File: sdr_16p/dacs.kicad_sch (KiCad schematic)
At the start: 2 parts, among them U15 HMC7043LP7FE, U9 AD9508BCPZ

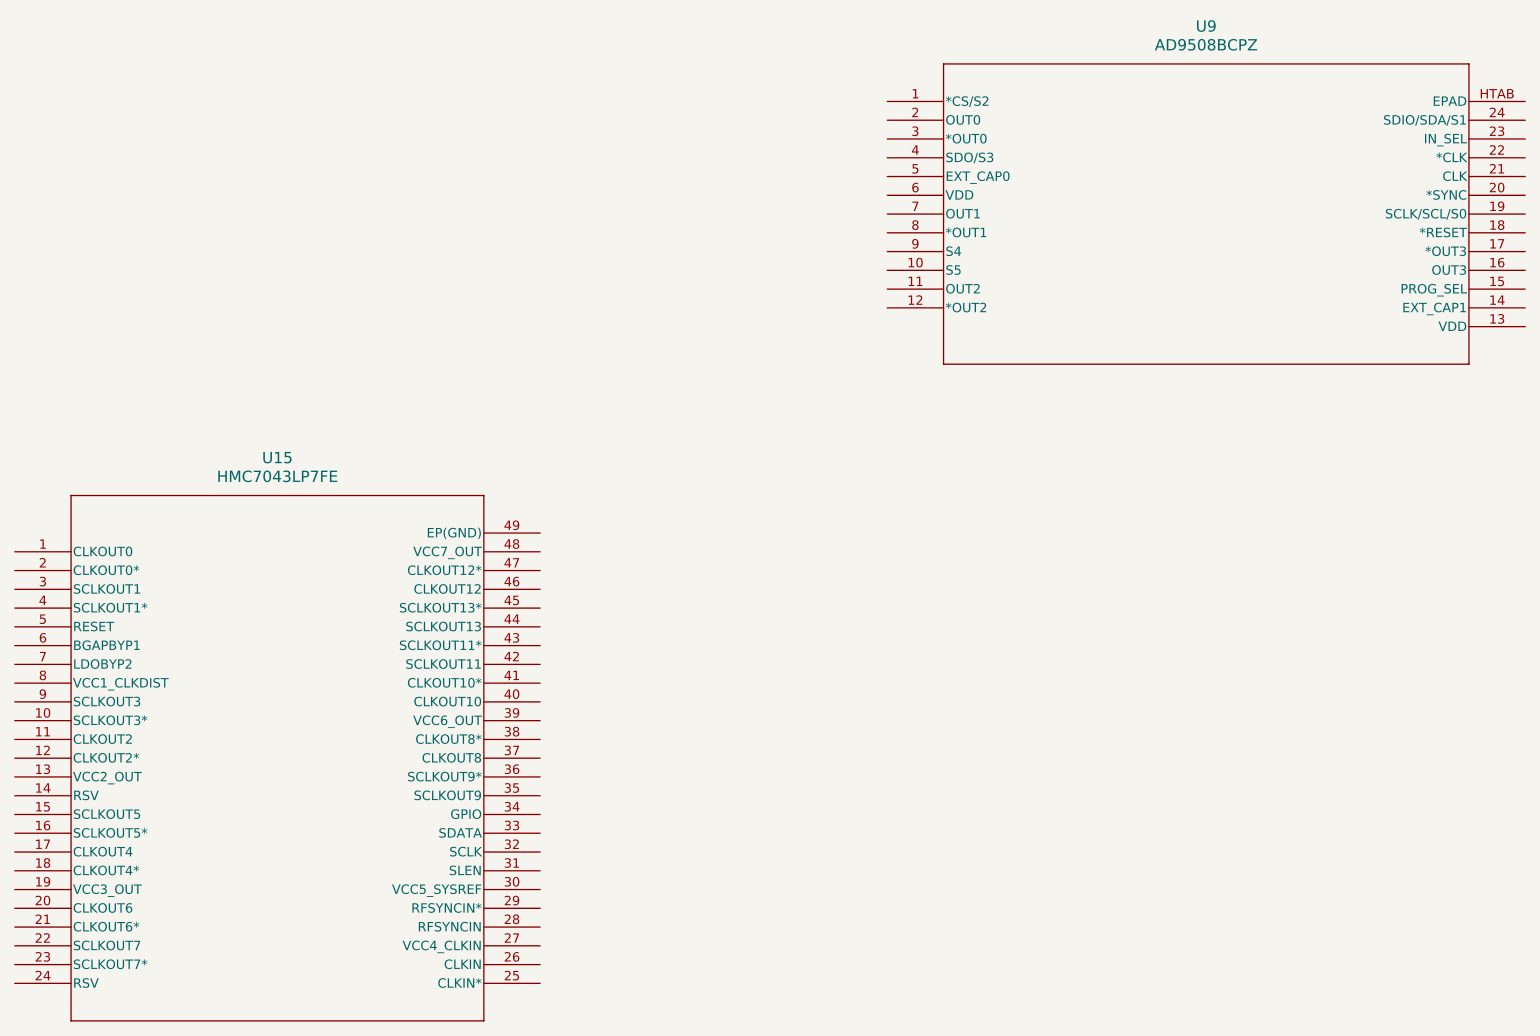
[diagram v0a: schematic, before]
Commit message: back to 16 phases
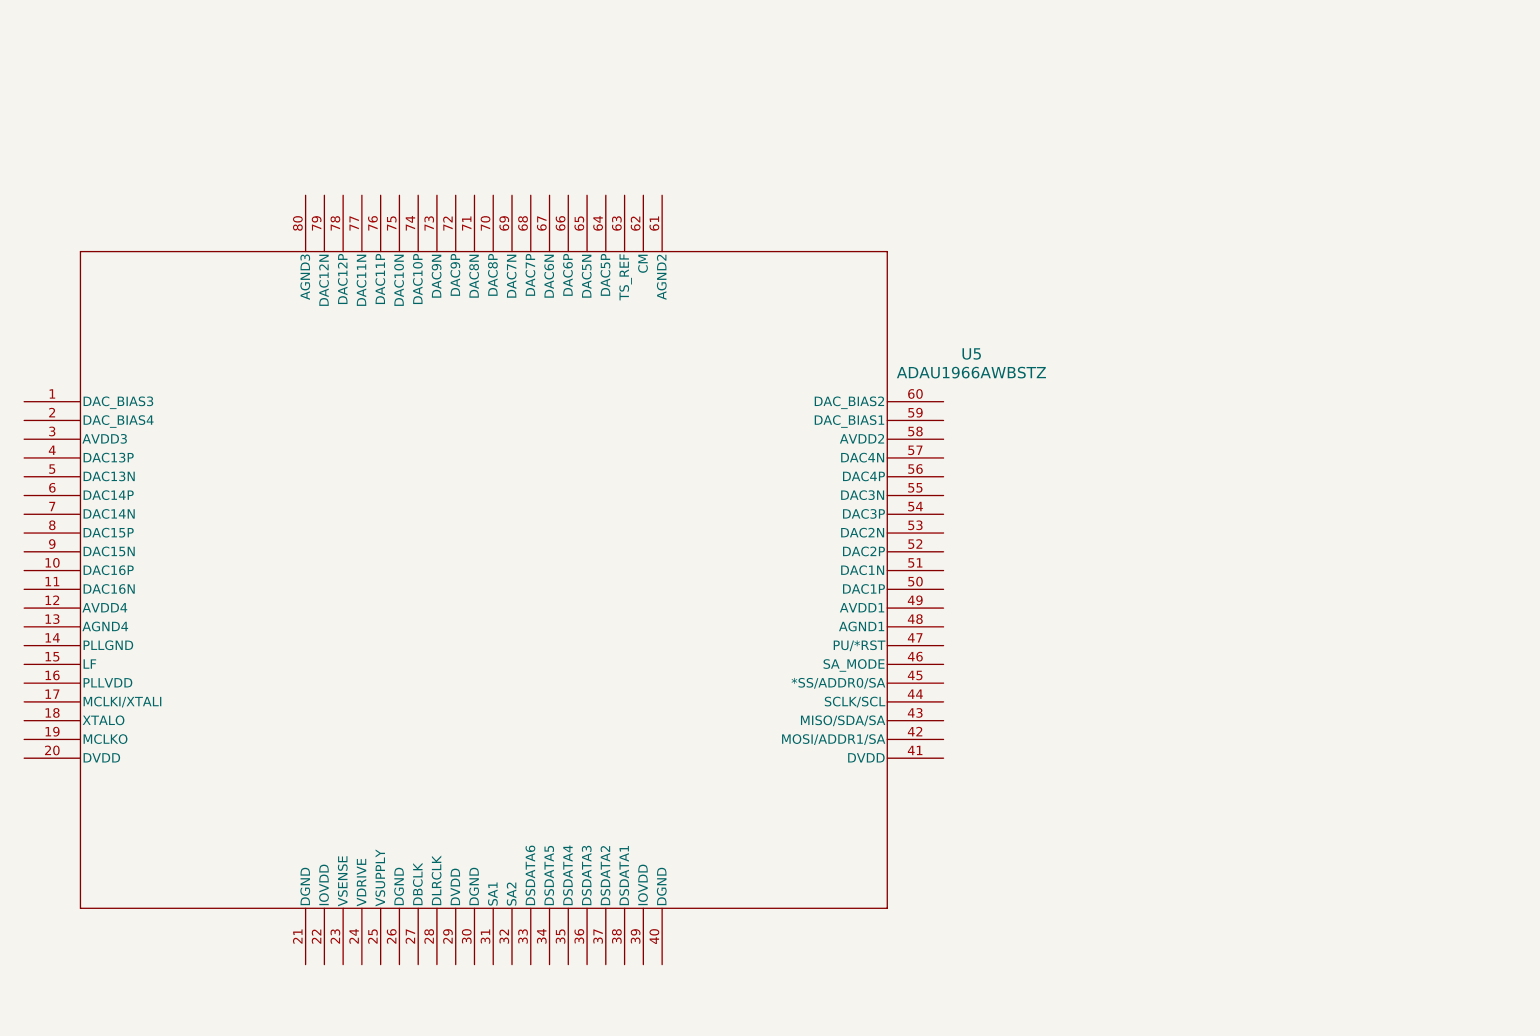
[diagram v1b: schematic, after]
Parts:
- removed U15: HMC7043LP7FE, HCP_48_1_ADI, symbol HMC7043:HMC7043LP7FE
- removed U9: AD9508BCPZ, CP_24_7_ADI, symbol AD9508:AD9508BCPZ
- added U5: ADAU1966AWBSTZ, ST_80_2_ADI, symbol ADAU1966:ADAU1966AWBSTZ
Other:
- title: Clock Tree -> Transmit DACs
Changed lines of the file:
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@@
 	(paper "B")
 	(title_block
-		(title "Clock Tree")
-		(date "2025-12-31")
+		(title "Transmit DACs")
+		(date "2026-01-02")
 		(rev "0.0")
 		(company "Andy McCann KA3KAF and Doug McCann KA3KAG")
 	)
 	(symbol
-		(lib_id "HMC7043:HMC7043LP7FE")
-		(at 142.24 113.03 0)
+		(lib_id "ADAU1966:ADAU1966AWBSTZ")
+		(at 143.51 92.71 0)
 		(unit 1)
 		(exclude_from_sim no)
@@
 		(dnp no)
 		(fields_autoplaced yes)
-		(property "Reference" "U15"
-			(at 177.8 100.33 0)
+		(property "Reference" "U5"
+			(at 271.78 86.2898 0)
 			(effects
 				(font
@@
 			)
 		)
-		(property "Value" "HMC7043LP7FE"
-			(at 177.8 102.87 0)
+		(property "Value" "ADAU1966AWBSTZ"
+			(at 271.78 88.8298 0)
 			(effects
 				(font
@@
 			)
 		)
-		(property "Footprint" "HCP_48_1_ADI"
-			(at 142.24 113.03 0)
+		(property "Footprint" "ST_80_2_ADI"
+			(at 143.51 92.71 0)
 			(effects
 				(font
@@
 			)
 		)
-		(property "Datasheet" "https://www.analog.com/media/en/technical-documentation/data-sheets/HMC7043.pdf"
-			(at 142.24 113.03 0)
+		(property "Datasheet" "https://www.analog.com/media/en/technical-documentation/data-sheets/ADAU1966A.pdf"
+			(at 143.51 92.71 0)
 			(effects
 				(font
@@
 		)
 		(property "Description" ""
-			(at 142.24 113.03 0)
+			(at 143.51 92.71 0)
 			(effects
 				(font
@@
 			)
 		)
+		(pin "35"
+		)
+		(pin "44"
+		)
+		(pin "4"
+		)
+		(pin "18"
+		)
+		(pin "49"
+		)
+		(pin "41"
+		)
+		(pin "47"
+		)
+		(pin "62"
+		)
+		(pin "8"
+		)
+		(pin "53"
+		)
+		(pin "14"
+		)
+		(pin "15"
+		)
+		(pin "6"
+		)
+		(pin "58"
+		)
+		(pin "56"
+		)
+		(pin "59"
+		)
+		(pin "48"
+		)
+		(pin "3"
+		)
+		(pin "52"
+		)
+		(pin "63"
+		)
+		(pin "37"
+		)
+		(pin "36"
+		)
+		(pin "65"
+		)
+		(pin "46"
+		)
+		(pin "51"
+		)
+		(pin "55"
+		)
+		(pin "60"
+		)
+		(pin "30"
+		)
+		(pin "42"
+		)
+		(pin "76"
+		)
+		(pin "75"
+		)
+		(pin "68"
+		)
+		(pin "31"
+		)
+		(pin "64"
+		)
+		(pin "5"
+		)
+		(pin "77"
+		)
+		(pin "71"
+		)
+		(pin "69"
+		)
+		(pin "73"
+		)
+		(pin "78"
+		)
+		(pin "10"
+		)
+		(pin "54"
+		)
+		(pin "2"
+		)
+		(pin "1"
+		)
+		(pin "11"
+		)
+		(pin "12"
+		)
+		(pin "32"
+		)
+		(pin "80"
+		)
+		(pin "21"
+		)
+		(pin "79"
+		)
+		(pin "9"
+		)
+		(pin "70"
+		)
+		(pin "24"
+		)
+		(pin "45"
+		)
+		(pin "29"
+		)
+		(pin "7"
+		)
+		(pin "43"
+		)
+		(pin "17"
+		)
+		(pin "22"
+		)
+		(pin "23"
+		)
+		(pin "67"
+		)
+		(pin "72"
+		)
+		(pin "26"
+		)
+		(pin "13"
+		)
 		(pin "27"
 		)
-		(pin "5"
+		(pin "57"
+		)
+		(pin "38"
+		)
+		(pin "50"
+		)
+		(pin "74"
+		)
+		(pin "25"
+		)
+		(pin "61"
+		)
+		(pin "28"
+		)
+		(pin "66"
+		)
+		(pin "20"
+		)
+		(pin "16"
+		)
+		(pin "19"
+		)
+		(pin "40"
 		)
 		(pin "34"
 		)
-		(pin "26"
-		)
-		(pin "2"
-		)
-		(pin "25"
-		)
-		(pin "47"
-		)
-		(pin "9"
-		)
-		(pin "36"
-		)
-		(pin "6"
-		)
-		(pin "23"
-		)
-		(pin "4"
-		)
-		(pin "45"
-		)
-		(pin "18"
-		)
-		(pin "44"
-		)
-		(pin "42"
-		)
-		(pin "16"
-		)
-		(pin "38"
-		)
-		(pin "28"
-		)
-		(pin "40"
-		)
-		(pin "29"
-		)
-		(pin "24"
-		)
-		(pin "48"
-		)
-		(pin "21"
+		(pin "39"
 		)
 		(pin "33"
-		)
-		(pin "20"
-		)
-		(pin "39"
-		)
-		(pin "13"
-		)
-		(pin "41"
-		)
-		(pin "17"
-		)
-		(pin "1"
-		)
-		(pin "31"
-		)
-		(pin "3"
-		)
-		(pin "8"
-		)
-		(pin "35"
-		)
-		(pin "7"
-		)
-		(pin "43"
-		)
-		(pin "32"
-		)
-		(pin "14"
-		)
-		(pin "15"
-		)
-		(pin "37"
-		)
-		(pin "12"
-		)
-		(pin "49"
-		)
-		(pin "19"
-		)
-		(pin "22"
-		)
-		(pin "11"
-		)
-		(pin "10"
-		)
-		(pin "46"
-		)
-		(pin "30"
 		)
 		(instances
 			(project ""
-				(path "/fe42ca2f-2bb8-4d5a-9e84-807788ed632f/79014999-6129-417a-b831-cb9e4a5873fe"
-					(reference "U15")
+				(path "/fe42ca2f-2bb8-4d5a-9e84-807788ed632f/1097e363-2947-4914-97f0-a09e0bb38c3a"
+					(reference "U5")
 					(unit 1)
 				)
-			)
-		)
-	)
-	(symbol
-		(lib_id "AD9508:AD9508BCPZ")
-		(at 260.35 52.07 0)
-		(unit 1)
-		(exclude_from_sim no)
-		(in_bom yes)
-		(on_board yes)
-		(dnp no)
-		(fields_autoplaced yes)
-		(property "Reference" "U9"
-			(at 303.53 41.91 0)
-			(effects
-				(font
-					(size 1.524 1.524)
-				)
-			)
-		)
-		(property "Value" "AD9508BCPZ"
-			(at 303.53 44.45 0)
-			(effects
-				(font
-					(size 1.524 1.524)
-				)
-			)
-		)
-		(property "Footprint" "CP_24_7_ADI"
-			(at 260.35 52.07 0)
-			(effects
-				(font
-					(size 1.27 1.27)
-					(italic yes)
-				)
-				(hide yes)
-			)
-		)
-		(property "Datasheet" "https://www.analog.com/media/en/technical-documentation/data-sheets/AD9508.pdf"
-			(at 260.35 52.07 0)
-			(effects
-				(font
-					(size 1.27 1.27)
-					(italic yes)
-				)
-				(hide yes)
-			)
-		)
-		(property "Description" ""
-			(at 260.35 52.07 0)
-			(effects
-				(font
-					(size 1.27 1.27)
-				)
-				(hide yes)
-			)
-		)
-		(pin "9"
-		)
-		(pin "17"
-		)
-		(pin "11"
-		)
-		(pin "7"
-		)
-		(pin "14"
-		)
-		(pin "8"
-		)
-		(pin "19"
-		)
-		(pin "23"
-		)
-		(pin "20"
-		)
-		(pin "24"
-		)
-		(pin "12"
-		)
-		(pin "1"
-		)
-		(pin "2"
-		)
-		(pin "15"
-		)
-		(pin "HTAB"
-		)
-		(pin "21"
-		)
-		(pin "16"
-		)
-		(pin "3"
-		)
-		(pin "6"
-		)
-		(pin "13"
-		)
-		(pin "10"
-		)
-		(pin "22"
-		)
-		(pin "18"
-		)
-		(pin "5"
-		)
-		(pin "4"
-		)
-		(instances
-			(project ""
-				(path "/fe42ca2f-2bb8-4d5a-9e84-807788ed632f/79014999-6129-417a-b831-cb9e4a5873fe"
-					(reference "U9")
-					(unit 1)
-				)
